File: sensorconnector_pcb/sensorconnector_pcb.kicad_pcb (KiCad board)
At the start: 2 copper layers, 61 x 20.3 mm, 4 parts, among them J1 RJ45_Shielded, J2 Conn_01x04_Male, J3 RJ45_Shielded

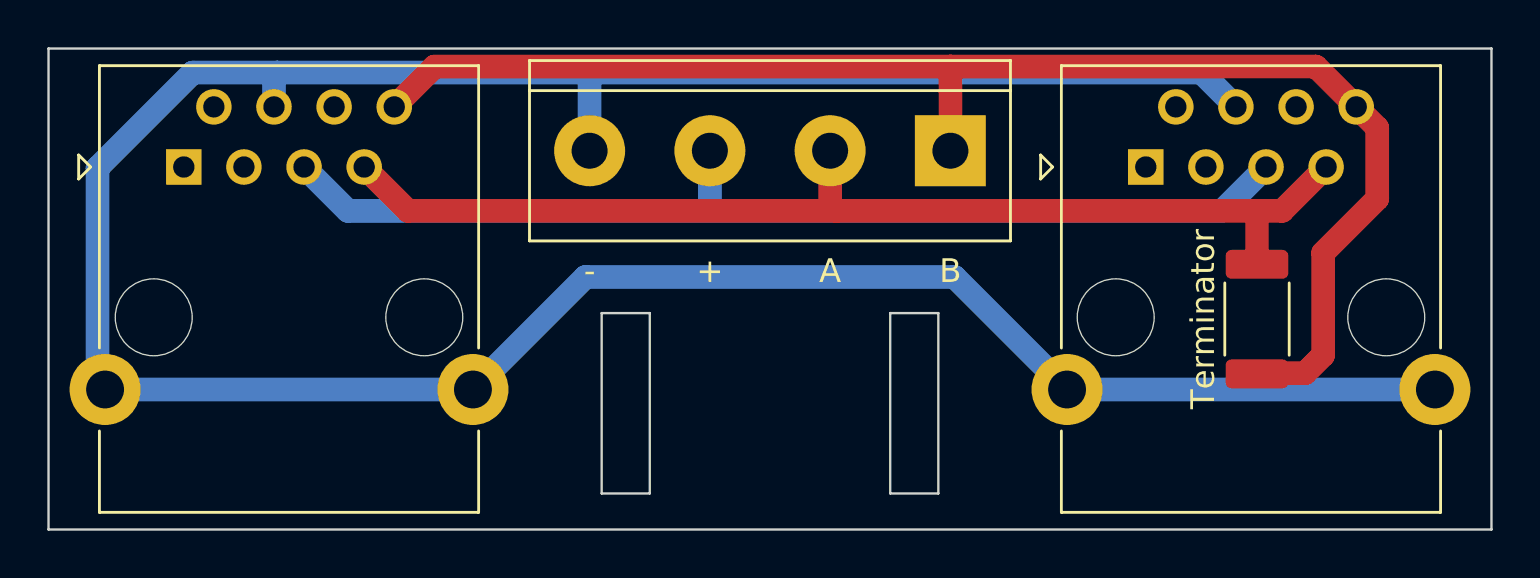
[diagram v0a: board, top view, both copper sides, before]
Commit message: Updated to a multiplexed analog humidity sensor connector
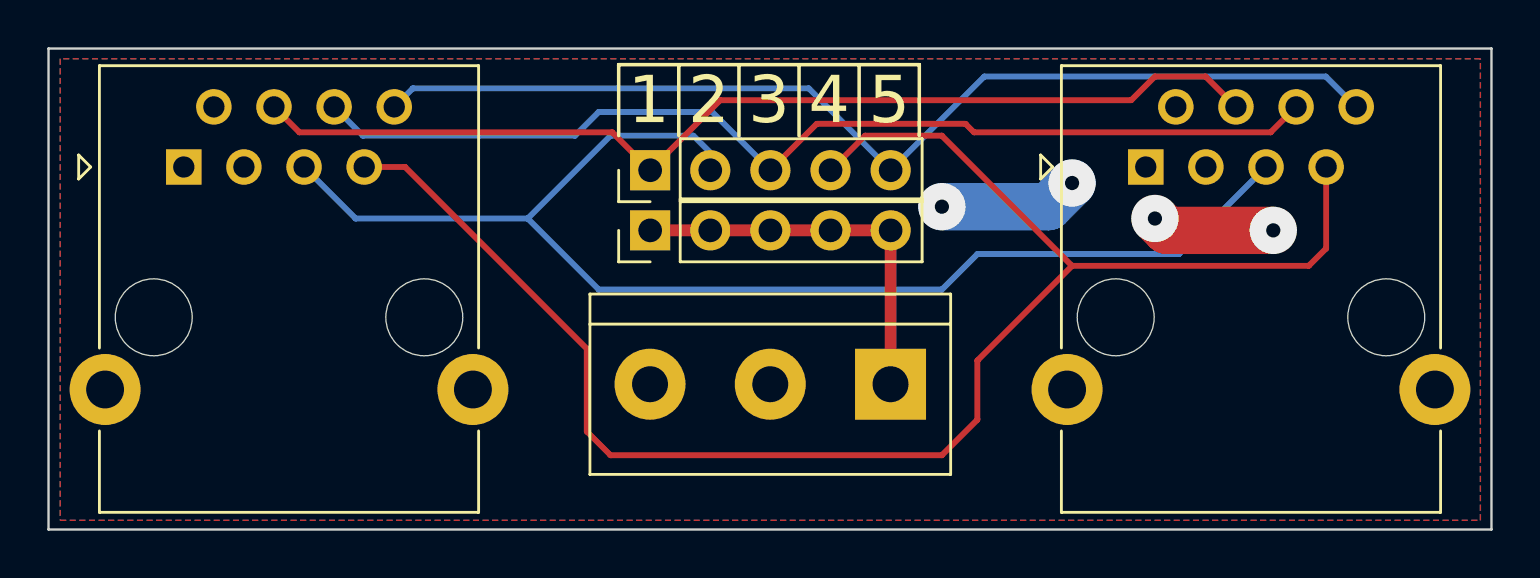
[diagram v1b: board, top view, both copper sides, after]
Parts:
- removed Terminator: 120Ω, Resistor_SMD:R_2010_5025Metric
- added J4: Conn_01x05_Pin, Connector_PinHeader_2.54mm:PinHeader_1x05_P2.54mm_Vertical, F.Cu at (121.2, 75.5)
- added J5: Conn_01x03_Pin, TerminalBlock:TerminalBlock_bornier-3_P5.08mm, F.Cu at (131.3, 82.0)
- J2: value Conn_01x04_Male -> Conn_01x05_Pin; footprint TerminalBlock:TerminalBlock_bornier-4_P5.08mm -> Connector_PinHeader_2.54mm:PinHeader_1x05_P2.54mm_Vertical
- moved J2 12.7 mm to (121.2, 73.0), turned to 90 degrees
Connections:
- J1 pad 1: unconnected-(J1-Pad1) -> +5V
- J1 pad 2: unconnected-(J1-Pad2) -> GND
- J1 pad 3: unconnected-(J1-Pad3) -> GND
- J1 pad 4: Net-(J1-Pad4) -> Net-(J2-Pin_1)
- J1 pad 5: Net-(J1-Pad5) -> Net-(J2-Pin_2)
- J1 pad 6: unconnected-(J1-Pad6) -> Net-(J2-Pin_3)
- J1 pad 7: Net-(J1-Pad7) -> Net-(J2-Pin_4)
- J1 pad 8: Net-(J1-Pad8) -> Net-(J2-Pin_5)
- J1 pad SH: Net-(J1-Pad4) -> GND
- J2 pad 1: Net-(J1-Pad8) -> Net-(J2-Pin_1)
- J2 pad 2: Net-(J1-Pad7) -> Net-(J2-Pin_2)
- J2 pad 3: Net-(J1-Pad5) -> Net-(J2-Pin_3)
- J2 pad 4: Net-(J1-Pad4) -> Net-(J2-Pin_4)
- J3 pad 1: unconnected-(J3-Pad1) -> +5V
- J3 pad 2: unconnected-(J3-Pad2) -> GND
- J3 pad 3: unconnected-(J3-Pad3) -> GND
- J3 pad 4: Net-(J1-Pad4) -> Net-(J2-Pin_1)
- J3 pad 5: Net-(J1-Pad5) -> Net-(J2-Pin_2)
- J3 pad 6: unconnected-(J3-Pad6) -> Net-(J2-Pin_3)
- J3 pad 7: Net-(J1-Pad7) -> Net-(J2-Pin_4)
- J3 pad 8: Net-(J1-Pad8) -> Net-(J2-Pin_5)
- J3 pad SH: Net-(J1-Pad4) -> GND
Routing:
- net Net-(J1-Pad4): track 124.8 -> 0.00 mm
- net Net-(J2-Pin_4): track 0.00 -> 69.3 mm
- net Net-(J1-Pad8): track 60.5 -> 0.00 mm
- net Net-(J2-Pin_2): track 0.00 -> 55.1 mm
- net Net-(J1-Pad7): track 47.1 -> 0.00 mm
- net Net-(J1-Pad5): track 44.7 -> 0.00 mm
- net Net-(J2-Pin_5): track 0.00 -> 44.6 mm
- net Net-(J2-Pin_3): track 0.00 -> 44.0 mm
- net Net-(J2-Pin_1): track 0.00 -> 43.9 mm
- net Net-(J4-Pin_1): track 0.00 -> 16.7 mm
- net +5V: track 0.00 -> 5.91 mm, vias 0 -> 2
- net GND: track 0.00 -> 5.21 mm, vias 0 -> 2
- added copper zone on F.Cu, net +5V
- added copper zone on B.Cu, net GND
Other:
- outline, holes or cut-outs redrawn
- board text added: "1"
- board text added: "2"
- board text added: "3"
- board text added: "4"
- board text added: "5"
- board text removed: "+"
- board text removed: "-"
- board text removed: "-: +: A: B:"
- board text removed: "A"
- board text removed: "B"
- board text removed: "Blue Blue/White Brown/White Brown"
- board text removed: "RS-485 Connector"
